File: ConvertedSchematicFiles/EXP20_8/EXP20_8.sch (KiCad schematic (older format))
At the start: 18 parts, among them Q1 Q2N2222, Q2 Q2N2222

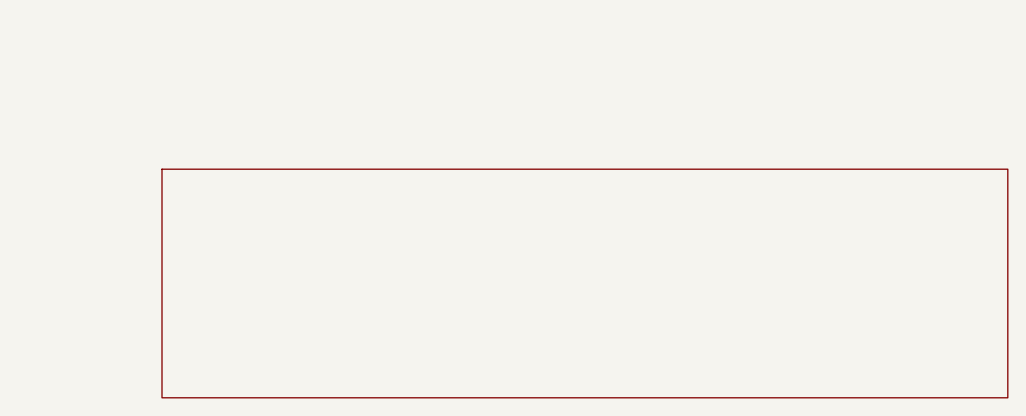
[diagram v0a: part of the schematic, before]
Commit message: Excluded some components. These no longer appear after conversion. When calling shell commands, filenames are in "quotes"
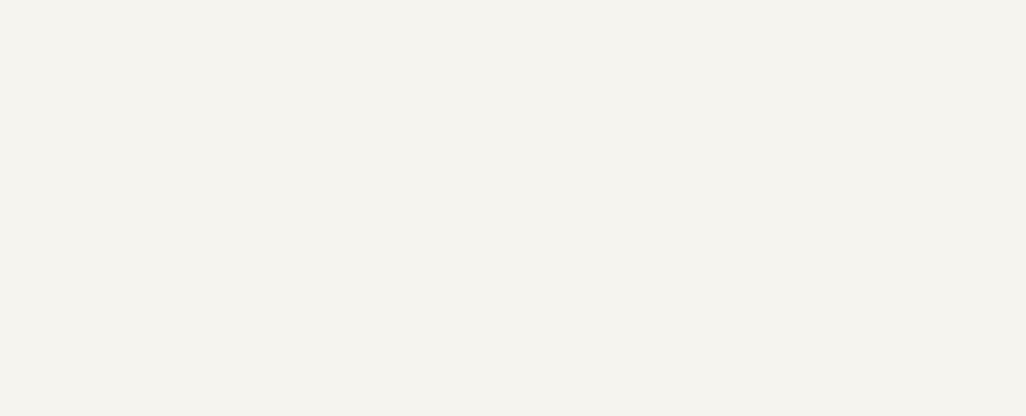
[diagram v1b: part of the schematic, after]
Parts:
- removed titleblk: titleblk, symbol TITLEBLK_PSPICE
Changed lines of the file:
@@
 	0    -1    1    0
-$EndComp
-$Comp
-L TITLEBLK_PSPICE titleblk
-U 1 1 20383426
-P 9700 7200
-F 0 "titleblk" H 19400 14400 30  0001 L CNN
-F 1 "titleblk" H 19400 14480 30  0001 L CNN
-	1    9700 7200
-	1    0    0    1
 $EndComp
 Wire Wire Line

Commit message: Ports issue fixed. Now annotation for ports is #PWR? function added "itos"
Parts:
- removed GND_ANALOG (x5): GND_ANALOG, symbol GND_ANALOG_PSPICE
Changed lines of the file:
@@
 $EndDescr
 $Comp
-L GND_ANALOG_PSPICE GND_ANALOG
+L GND_ANALOG_PSPICE #PWR1
 U 1 1 14289383
 P 400 4400
-F 0 "GND_ANALOG" H 800 8800 30  0001 L CNN
+F 0 "#PWR1" H 800 8800 30  0001 L CNN
 F 1 "GND_ANALOG" H 800 8880 30  0001 L CNN
 	1    400 4400
@@
 $EndComp
 $Comp
-L GND_ANALOG_PSPICE GND_ANALOG
+L GND_ANALOG_PSPICE #PWR2
 U 1 1 46930886
 P 3400 5200
-F 0 "GND_ANALOG" H 6800 10400 30  0001 L CNN
+F 0 "#PWR2" H 6800 10400 30  0001 L CNN
 F 1 "GND_ANALOG" H 6800 10480 30  0001 L CNN
 	1    3400 5200
@@
 $EndComp
 $Comp
-L GND_ANALOG_PSPICE GND_ANALOG
+L GND_ANALOG_PSPICE #PWR3
 U 1 1 71692777
 P 4100 3000
-F 0 "GND_ANALOG" H 8200 6000 30  0001 L CNN
+F 0 "#PWR3" H 8200 6000 30  0001 L CNN
 F 1 "GND_ANALOG" H 8200 6080 30  0001 L CNN
 	1    4100 3000
@@
 $EndComp
 $Comp
-L GND_ANALOG_PSPICE GND_ANALOG
+L GND_ANALOG_PSPICE #PWR4
 U 1 1 14636915
 P 2300 4400
-F 0 "GND_ANALOG" H 4600 8800 30  0001 L CNN
+F 0 "#PWR4" H 4600 8800 30  0001 L CNN
 F 1 "GND_ANALOG" H 4600 8880 30  0001 L CNN
 	1    2300 4400
@@
 $EndComp
 $Comp
-L GND_ANALOG_PSPICE GND_ANALOG
+L GND_ANALOG_PSPICE #PWR5
 U 1 1 77747793
 P 1900 4200
-F 0 "GND_ANALOG" H 3800 8400 30  0001 L CNN
+F 0 "#PWR5" H 3800 8400 30  0001 L CNN
 F 1 "GND_ANALOG" H 3800 8480 30  0001 L CNN
 	1    1900 4200

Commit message: Added LICENSE.txt
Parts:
- V3: value VPULSE -> PULSE
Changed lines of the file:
@@
 $EndDescr
 $Comp
-L GND_ANALOG_PSPICE #PWR1
+L AGND #PWR1
 U 1 1 14289383
 P 400 4400
@@
 $EndComp
 $Comp
-L GND_ANALOG_PSPICE #PWR2
+L AGND #PWR2
 U 1 1 46930886
 P 3400 5200
@@
 $EndComp
 $Comp
-L GND_ANALOG_PSPICE #PWR3
+L AGND #PWR3
 U 1 1 71692777
 P 4100 3000
@@
 $EndComp
 $Comp
-L GND_ANALOG_PSPICE #PWR4
+L AGND #PWR4
 U 1 1 14636915
 P 2300 4400
@@
 $EndComp
 $Comp
-L GND_ANALOG_PSPICE #PWR5
+L AGND #PWR5
 U 1 1 77747793
 P 1900 4200
@@
 P 400 4000
 F 0 "V3" H 400 4000 30  0001 L CNN
-F 1 "VPULSE" H 400 4080 30  0001 L CNN
+F 1 "PULSE" H 400 4080 30  0001 L CNN
 	1    400 4000
 	1    0    0    1

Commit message: Orientation fix. Library components are now inverted, with +ve y axis going up. In Schematic files, +ve y axis is downwards. This is how the KiCad libraries are. As a result of the above fixed, the converted GND is now oriented correctly.
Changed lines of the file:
@@
 F 1 "GND_ANALOG" H 800 8880 30  0001 L CNN
 	1    400 4400
-	1    0    0    1
+	1    0    0    -1
 $EndComp
 $Comp
@@
 F 1 "GND_ANALOG" H 6800 10480 30  0001 L CNN
 	1    3400 5200
-	1    0    0    1
+	1    0    0    -1
 $EndComp
 $Comp
@@
 F 1 "GND_ANALOG" H 8200 6080 30  0001 L CNN
 	1    4100 3000
-	1    0    0    1
+	1    0    0    -1
 $EndComp
 $Comp
@@
 F 1 "GND_ANALOG" H 4600 8880 30  0001 L CNN
 	1    2300 4400
-	1    0    0    1
+	1    0    0    -1
 $EndComp
 $Comp
@@
 F 1 "GND_ANALOG" H 3800 8480 30  0001 L CNN
 	1    1900 4200
-	1    0    0    1
+	1    0    0    -1
 $EndComp
 $Comp
@@
 F 1 "100k" H 1400 3650 30  0000 L CNN
 	1    1400 3600
-	0    1    -1    0
+	0    -1    -1    0
 $EndComp
 $Comp
@@
 F 1 "20V" H 4100 2490 30  0000 C CNN
 	1    4100 2600
-	1    0    0    1
+	1    0    0    -1
 $EndComp
 $Comp
@@
 F 1 "10V" H 3400 5090 30  0000 C CNN
 	1    3400 5200
-	-1    0    0    -1
+	-1    0    0    1
 $EndComp
 $Comp
@@
 F 1 "10k" H 3400 4950 30  0000 L CNN
 	1    3400 4800
-	0    1    -1    0
+	0    -1    -1    0
 $EndComp
 $Comp
@@
 F 1 "5k" H 2300 3870 30  0000 L CNN
 	1    2300 3700
-	0    1    -1    0
+	0    -1    -1    0
 $EndComp
 $Comp
@@
 F 1 "0.1u" H 800 4150 30  0000 L CNN
 	1    800 4000
-	1    0    0    1
+	1    0    0    -1
 $EndComp
 $Comp
@@
 F 1 "PULSE" H 400 4080 30  0001 L CNN
 	1    400 4000
-	1    0    0    1
+	1    0    0    -1
 $EndComp
 $Comp
@@
 F 1 "10u" H 2900 2990 30  0000 L CNN
 	1    2900 3100
-	1    0    0    1
+	1    0    0    -1
 $EndComp
 $Comp
@@
 F 1 "0.1u" H 2300 4070 30  0000 L CNN
 	1    2300 4100
-	0    -1    1    0
+	0    1    1    0
 $EndComp
 $Comp
@@
 F 1 "Q2N2222" H 1700 4080 30  0001 L CNN
 	1    1700 4000
-	1    0    0    1
+	1    0    0    -1
 $EndComp
 $Comp
@@
 F 1 "Q2N2222" H 3200 3880 30  0001 L CNN
 	1    3200 3800
-	1    0    0    1
+	1    0    0    -1
 $EndComp
 $Comp
@@
 F 1 "D1N4148" H 2300 2680 30  0001 L CNN
 	1    2300 2600
-	0    -1    1    0
+	0    1    1    0
 $EndComp
 Wire Wire Line

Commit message: Removed the use of exec, wrote basename function, made integration with eSim easier.
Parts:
- added titleblk: titleblk, symbol titleblk_PSPICE
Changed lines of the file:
@@
-EESchema Schematic File Version 2  date Tuesday 08 June 1999 05:21:20 PM IST
+EESchema Schematic File Version 2  date
 LIBS:power
 LIBS:device
@@
 LIBS:contrib
 LIBS:valves
-LIBS:ConvertedSchematicFiles/EXP20_8-cache
 EELAYER 25  0
 EELAYER END
@@
 Sheet 1 1
 Title ""
-Date "08 Jun 1999"
+Date ""
 Rev ""
 Comp ""
@@
 	0    1    1    0
 $EndComp
+$Comp
+L titleblk_PSPICE titleblk
+U 1 1 20383426
+P 9700 7200
+F 0 "titleblk" H 19400 14400 30  0001 L CNN
+F 1 "titleblk" H 19400 14480 30  0001 L CNN
+	1    9700 7200
+	1    0    0    -1
+$EndComp
 Wire Wire Line
